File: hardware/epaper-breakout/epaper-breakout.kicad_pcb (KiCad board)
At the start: 2 copper layers, 100 x 40.5 mm, 90 parts, among them J1 XF2M-3315-1A, J2 C10418, J3 Conn_02x06_Counter_Clockwise, J4 ED060SC4, J5 Conn_01x01_Male, J6 Conn_01x01_Male, Q1 AO3401A, Q2 AO3401A, Q3 MMBT3904, Q4 MMBT3904, Q5 AO3401A, Q6 MMBT3904, U1 MCP1700-3302E_SOT23, U10 ED060SC7, U11 TP4056, U12 CH340C, U2 LT1945, U3 LT1945, U4 XC6206PxxxMR, U5 ESP32-WROVER, U6 ED060XC5, U7 LM358, U8 74HC4094-normal, U9 MCP9700AT-ETT

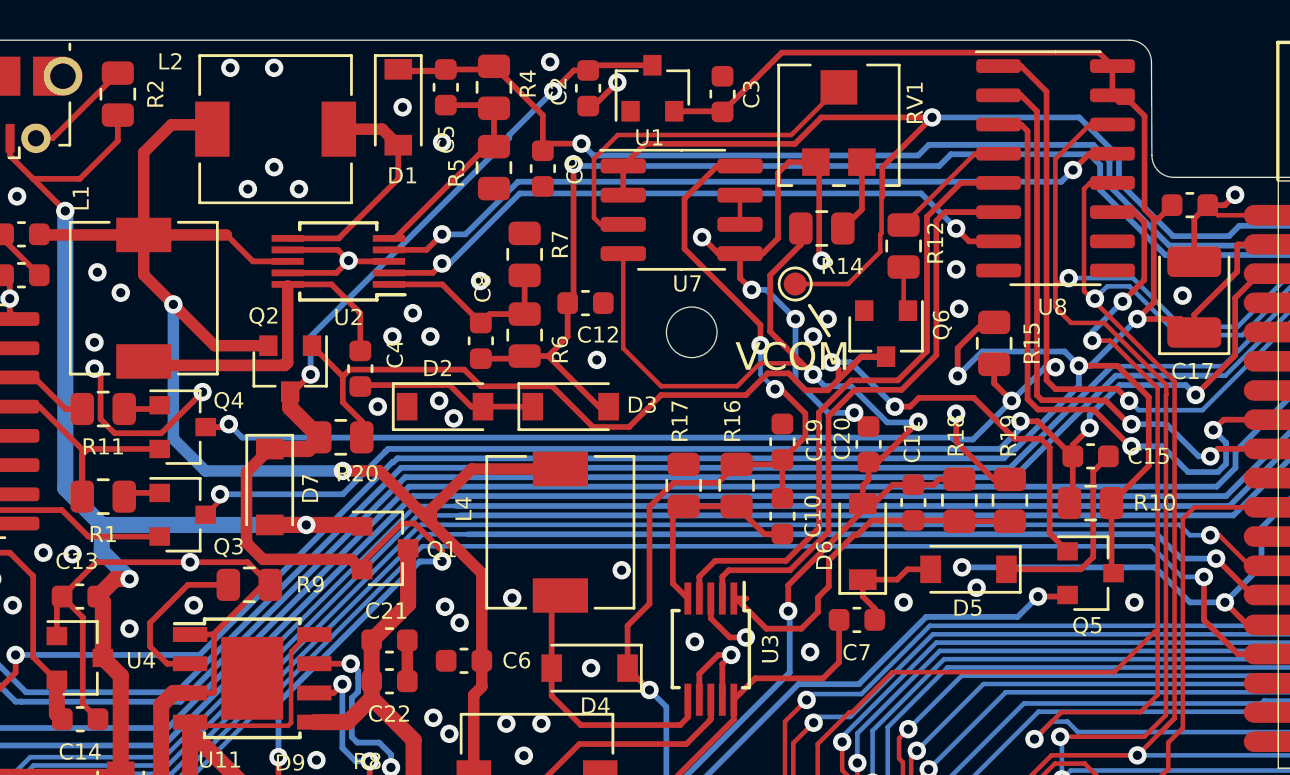
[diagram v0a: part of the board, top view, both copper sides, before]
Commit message: v5: fix mosfet orientation
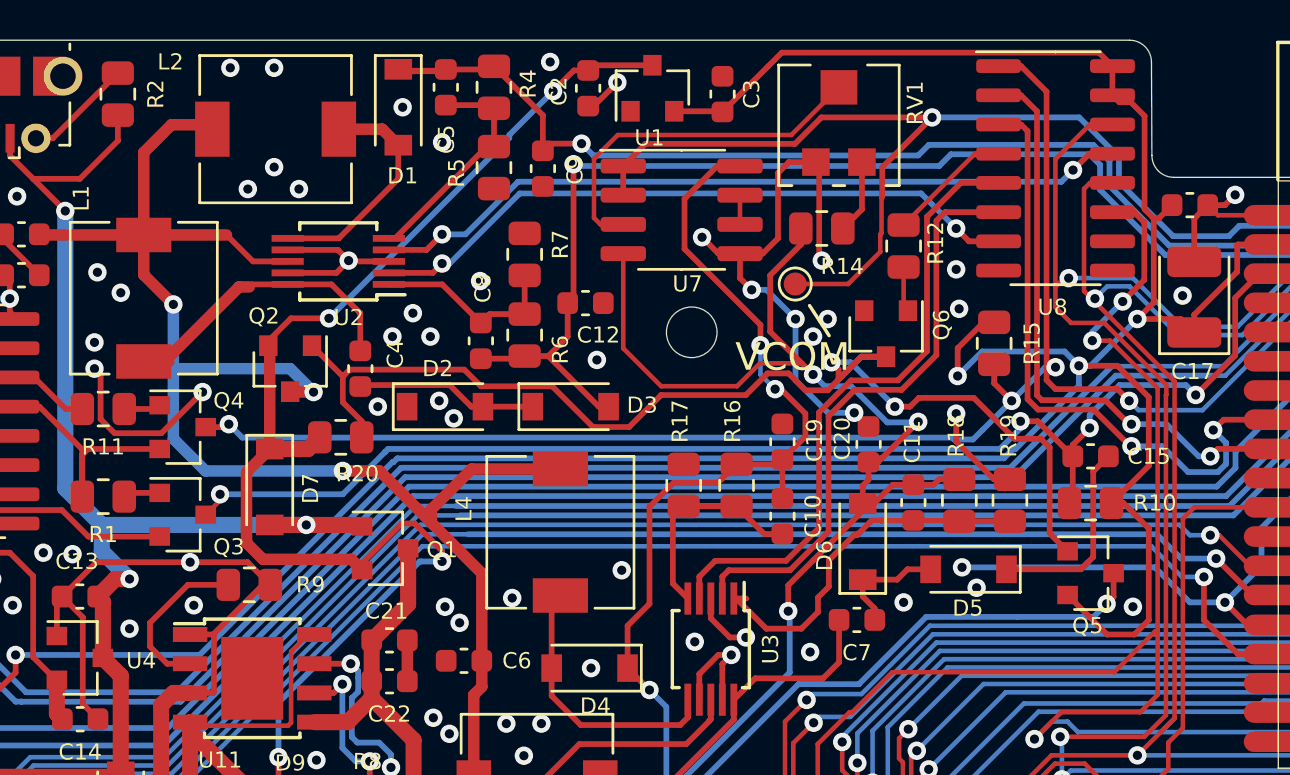
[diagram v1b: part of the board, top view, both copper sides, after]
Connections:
- Q2 pad 2: SW_VIN -> VIN
- Q2 pad 3: VIN -> SW_VIN
- Q5 pad 2: EPD_VDD -> /+3.3V
- Q5 pad 3: /+3.3V -> EPD_VDD
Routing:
- net Net-(C4-Pad2): track 24.6 -> 14.1 mm
- net /+3.3V: track 128.3 -> 135.8 mm
- net EPD_VDD: track 181.5 -> 184.5 mm
- net SW_VIN: track 77.5 -> 80.1 mm, vias 2 -> 3
- net VIN: track 61.8 -> 63.1 mm
